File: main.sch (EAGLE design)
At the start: 8 parts, among them X1 FH12-40S-0.5SH

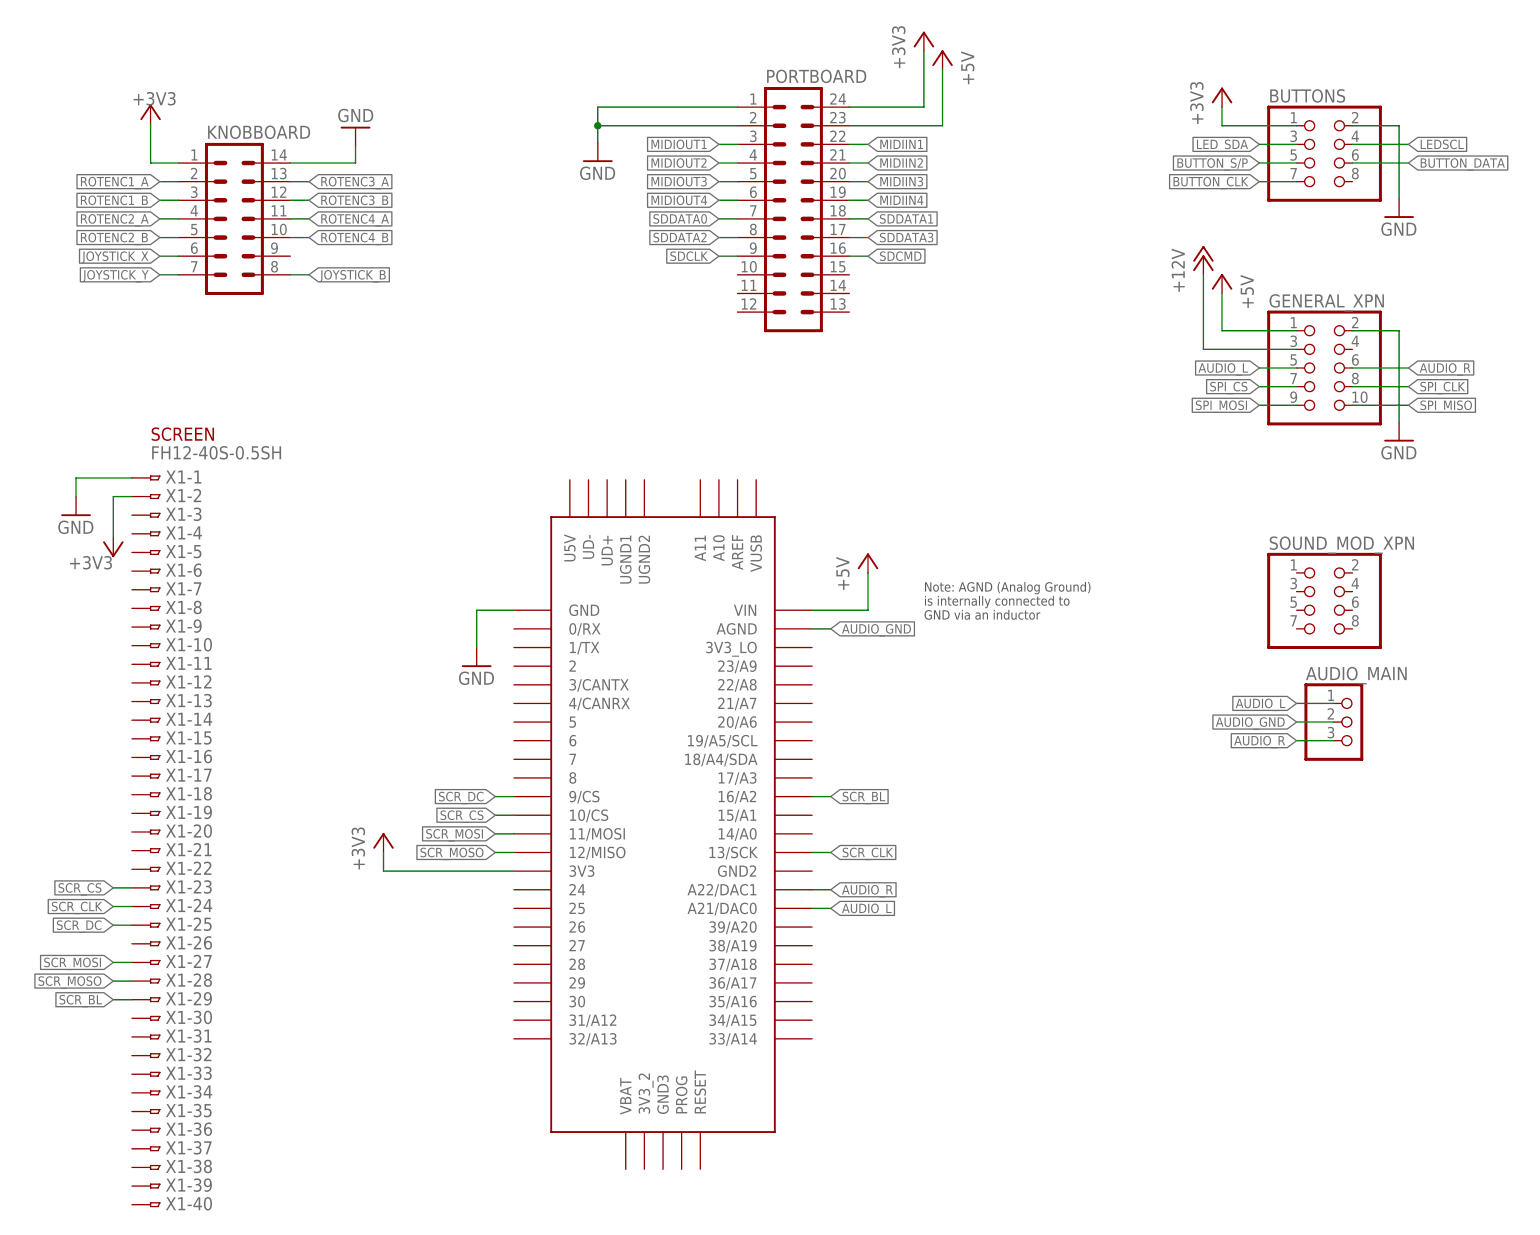
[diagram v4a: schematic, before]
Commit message: MIDI pinout connections, backup files cleanup, gitignore
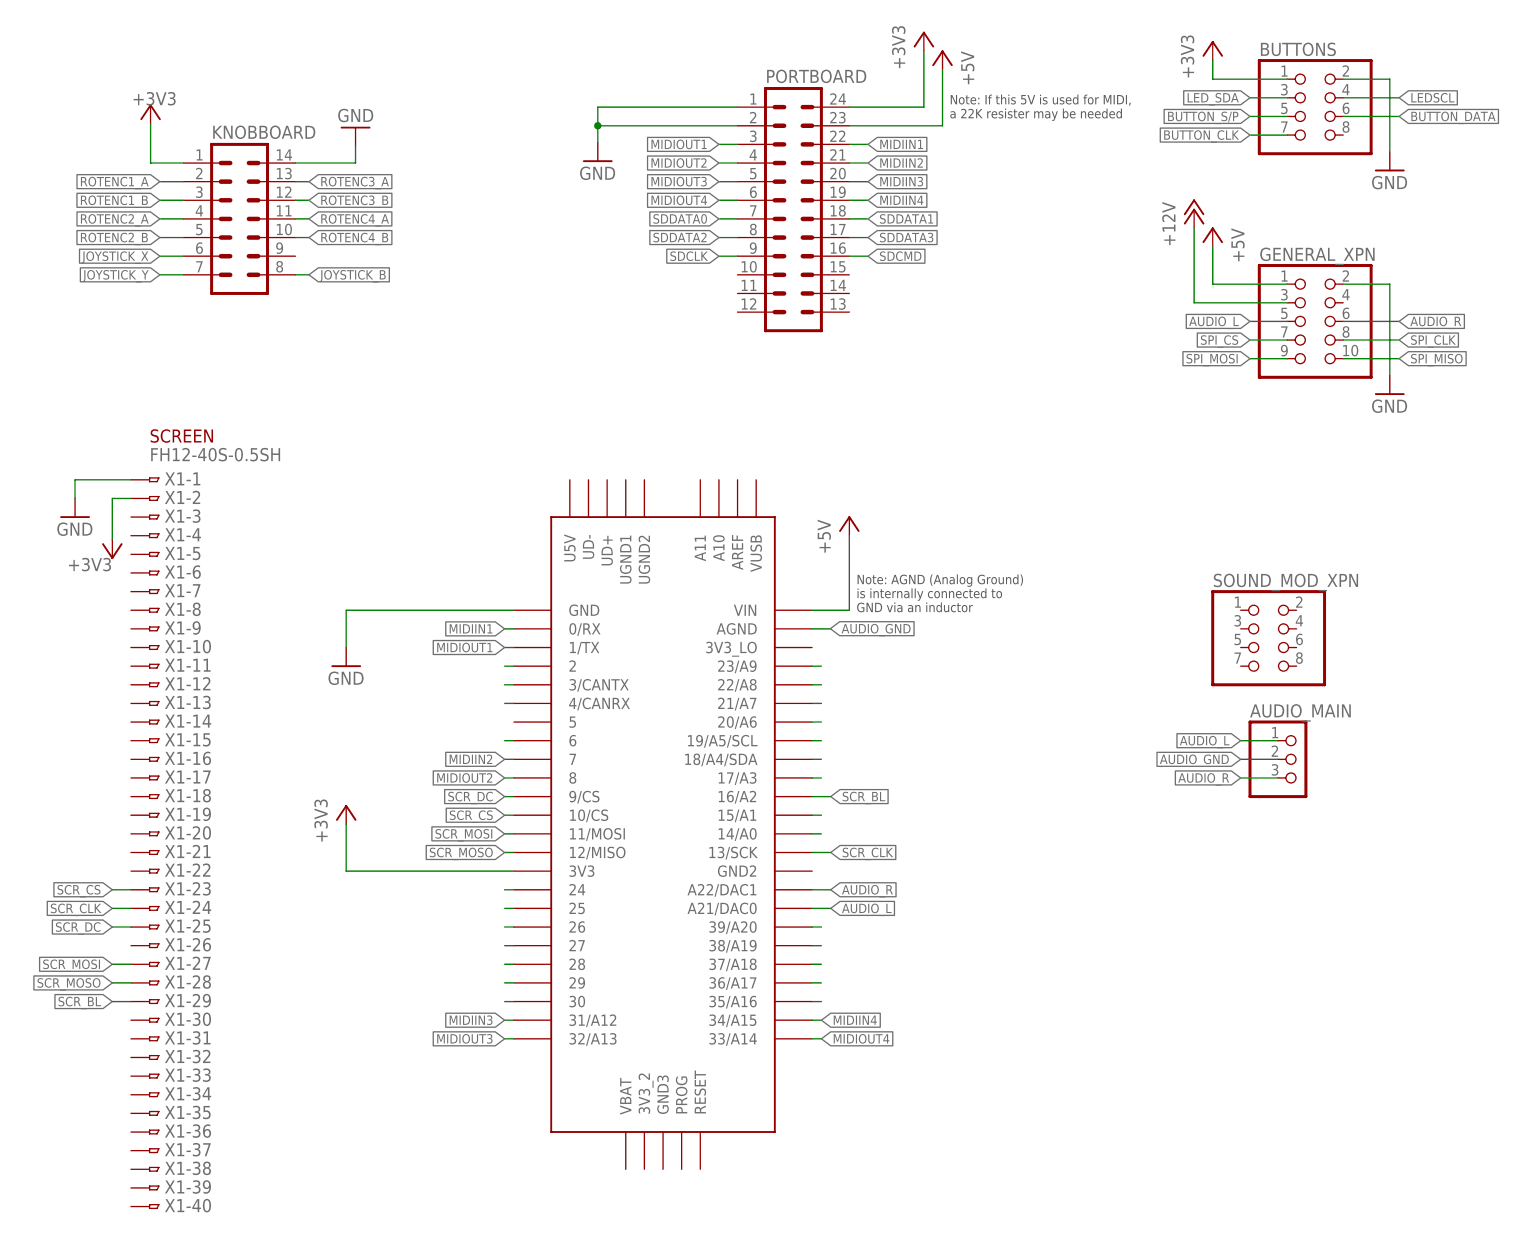
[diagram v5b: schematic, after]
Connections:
- new net N$10: U$1.25
- new net N$11: U$1.26
- new net N$12: U$1.27
- new net N$13: U$1.28
- new net N$14: U$1.29
- new net N$15: U$1.30
- new net N$18: U$1.23/A9
- new net N$19: U$1.22/A8
- new net N$20: U$1.21/A7
- new net N$21: U$1.20/A6
- new net N$22: U$1.19/A5/SCL
- new net N$23: U$1.18/A4/SDA
- new net N$24: U$1.17/A3
- new net N$25: U$1.15/A1
- new net N$26: U$1.14/A0
- new net N$3: U$1.2
- new net N$30: U$1.35/A16
- new net N$31: U$1.36/A17
- new net N$32: U$1.37/A18
- new net N$33: U$1.38/A19
- new net N$34: U$1.39/A20
- new net N$4: U$1.3/CANTX
- new net N$5: U$1.4/CANRX
- new net N$6: U$1.6
- new net N$9: U$1.24
- net MIDIIN1: now also U$1.0/RX
- net MIDIIN2: now also U$1.7
- net MIDIIN3: now also U$1.31/A12
- net MIDIIN4: now also U$1.34/A15
- net MIDIOUT1: now also U$1.1/TX
- net MIDIOUT2: now also U$1.8
- net MIDIOUT3: now also U$1.32/A13
- net MIDIOUT4: now also U$1.33/A14
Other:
- note added: "Note: If this 5V is used for MIDI, a 22K resister may be needed"
- moved on the sheet: AUDIO_MAIN, BUTTONS, GENERAL_XPN, KNOBBOARD, SOUND_MOD_XPN

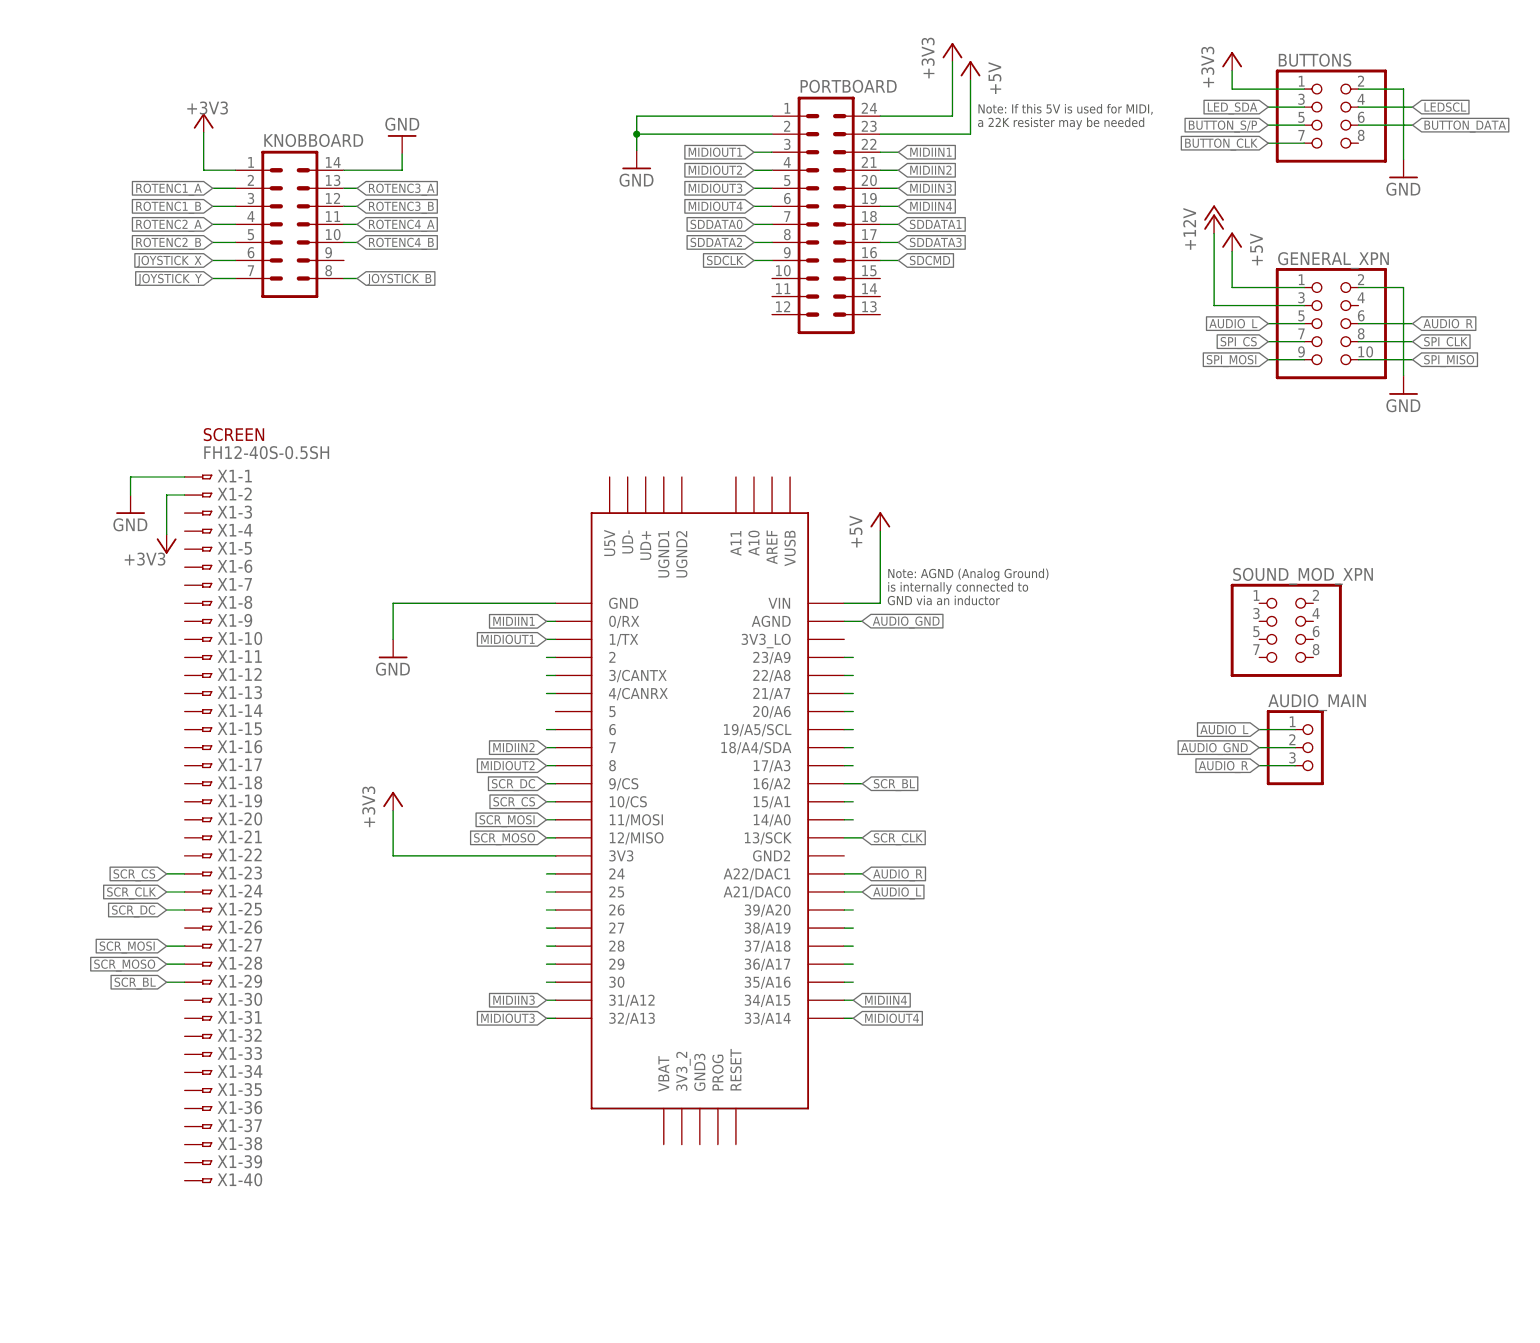
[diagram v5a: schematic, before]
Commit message: button expansion
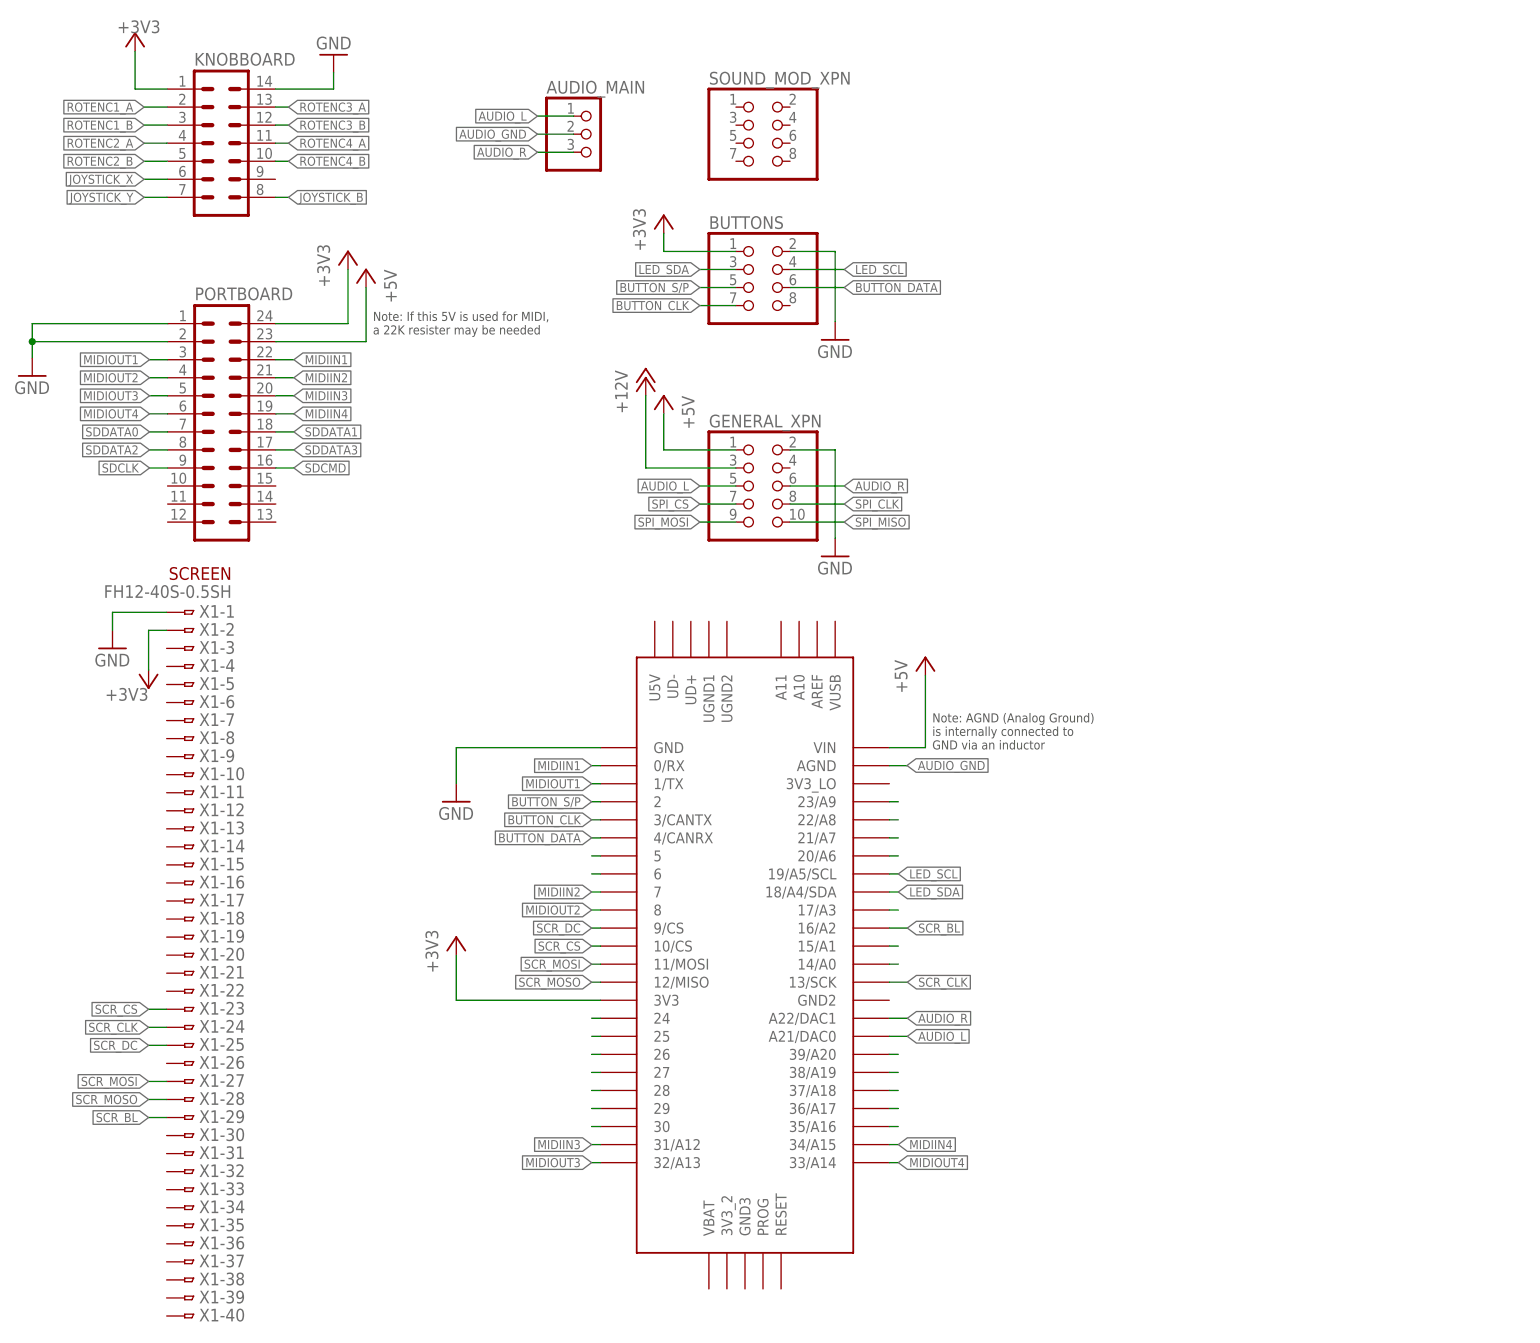
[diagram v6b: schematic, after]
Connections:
- removed net LEDSCL: BUTTONS.4
- removed net N$22: U$1.19/A5/SCL
- removed net N$23: U$1.18/A4/SDA
- removed net N$3: U$1.2
- removed net N$4: U$1.3/CANTX
- removed net N$5: U$1.4/CANRX
- new net LED_SCL: BUTTONS.4, U$1.19/A5/SCL
- new net N$1: U$1.5
- net BUTTON_CLK: now also U$1.3/CANTX
- net BUTTON_DATA: now also U$1.4/CANRX
- net BUTTON_S/P: now also U$1.2
- net LED_SDA: now also U$1.18/A4/SDA
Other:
- moved on the sheet: AUDIO_MAIN, BUTTONS, GENERAL_XPN, KNOBBOARD, PORTBOARD, SOUND_MOD_XPN, X1-1, X1-10, X1-11, X1-12, X1-13, X1-14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

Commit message: Milestone fully drafted
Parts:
- removed AUDIO_MAIN: (no value), pinhead:PINHD-1X3
- removed KNOBBOARD: (no value), con-dil:IC14PL
- removed SOUND_MOD_XPN: (no value), pinhead:PINHD-2X4
- removed X1: FH12-40S-0.5SH, con-hirose:FH12-40S-0.5SH
- added AUDIO_OUT: (no value), SparkFun-Connectors:CONN_03
- added J1: (no value), SparkFun-Connectors:CONN_08X2
- added SCR: FH12-40S-0.5SH, con-hirose:FH12-40S-0.5SH
- added SOUND_MODS: (no value), SparkFun-Connectors:CONN_04X2
- BUTTONS: device pinhead:PINHD-2X4 -> SparkFun-Connectors:CONN_04X2
- GENERAL_XPN: device pinhead:PINHD-2X5 -> SparkFun-Connectors:CONN_05X2PTH
- PORTBOARD: device con-dil:IC24PL -> SparkFun-Connectors:CONN_13X22X13
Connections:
- removed net N$13: U$1.28
- removed net N$14: U$1.29
- removed net N$15: U$1.30
- removed net N$18: U$1.23/A9
- removed net N$19: U$1.22/A8
- removed net N$24: U$1.17/A3
- removed net N$30: U$1.35/A16
- removed net N$31: U$1.36/A17
- removed net N$32: U$1.37/A18
- removed net N$33: U$1.38/A19
- removed net N$34: U$1.39/A20
- new net USBDATA+: PORTBOARD.13
- new net USBDATA-: PORTBOARD.14
- net +12V: now also PORTBOARD.26
- net +3V3: now also J1.1, PORTBOARD.2, SCR-2.1; no longer KNOBBOARD.1, PORTBOARD.24, X1-2.1
- net +5V: now also PORTBOARD.4; no longer PORTBOARD.23
- net AUDIO_GND: now also AUDIO_OUT.2; no longer AUDIO_MAIN.2
- net AUDIO_L: now also AUDIO_OUT.1; no longer AUDIO_MAIN.1
- net AUDIO_R: now also AUDIO_OUT.3; no longer AUDIO_MAIN.3
- net GND: now also J1.2, PORTBOARD.3, SCR-1.1; no longer KNOBBOARD.14, PORTBOARD.2, X1-1.1
- net JOYSTICK_B: now also J1.14, U$1.17/A3; no longer KNOBBOARD.8
- net JOYSTICK_X: now also J1.11, U$1.23/A9; no longer KNOBBOARD.6
- net JOYSTICK_Y: now also J1.13, U$1.22/A8; no longer KNOBBOARD.7
- net MIDIIN1: now also PORTBOARD.6; no longer PORTBOARD.22
- net MIDIIN2: now also PORTBOARD.8; no longer PORTBOARD.21
- net MIDIIN3: now also PORTBOARD.10; no longer PORTBOARD.20
- net MIDIIN4: now also PORTBOARD.12; no longer PORTBOARD.19
- net MIDIOUT1: now also PORTBOARD.5; no longer PORTBOARD.3
- net MIDIOUT2: now also PORTBOARD.7; no longer PORTBOARD.4
- net MIDIOUT3: now also PORTBOARD.9; no longer PORTBOARD.5
- net MIDIOUT4: now also PORTBOARD.11; no longer PORTBOARD.6
- net ROTENC1_A: now also J1.3, U$1.28; no longer KNOBBOARD.2
- net ROTENC1_B: now also J1.5, U$1.29; no longer KNOBBOARD.3
- net ROTENC2_A: now also J1.7, U$1.30; no longer KNOBBOARD.4
- net ROTENC2_B: now also J1.9, U$1.39/A20; no longer KNOBBOARD.5
- net ROTENC3_A: now also J1.4, U$1.38/A19; no longer KNOBBOARD.13
- net ROTENC3_B: now also J1.6, U$1.37/A18; no longer KNOBBOARD.12
- net ROTENC4_A: now also J1.8, U$1.36/A17; no longer KNOBBOARD.11
- net ROTENC4_B: now also J1.10, U$1.35/A16; no longer KNOBBOARD.10
- net SCR_BL: now also SCR-29.1; no longer X1-29.1
- net SCR_CLK: now also SCR-24.1; no longer X1-24.1
- net SCR_CS: now also SCR-23.1; no longer X1-23.1
- net SCR_DC: now also SCR-25.1; no longer X1-25.1
- net SCR_MOSI: now also SCR-27.1; no longer X1-27.1
- net SCR_MOSO: now also SCR-28.1; no longer X1-28.1
- net SDCLK: now also PORTBOARD.19; no longer PORTBOARD.9
- net SDCMD: now also PORTBOARD.20; no longer PORTBOARD.16
- net SDDATA0: now also PORTBOARD.15; no longer PORTBOARD.7
- net SDDATA1: now also PORTBOARD.16; no longer PORTBOARD.18
- net SDDATA2: now also PORTBOARD.17; no longer PORTBOARD.8
- net SDDATA3: now also PORTBOARD.18; no longer PORTBOARD.17
